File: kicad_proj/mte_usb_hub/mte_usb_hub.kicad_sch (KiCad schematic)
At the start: 3 parts

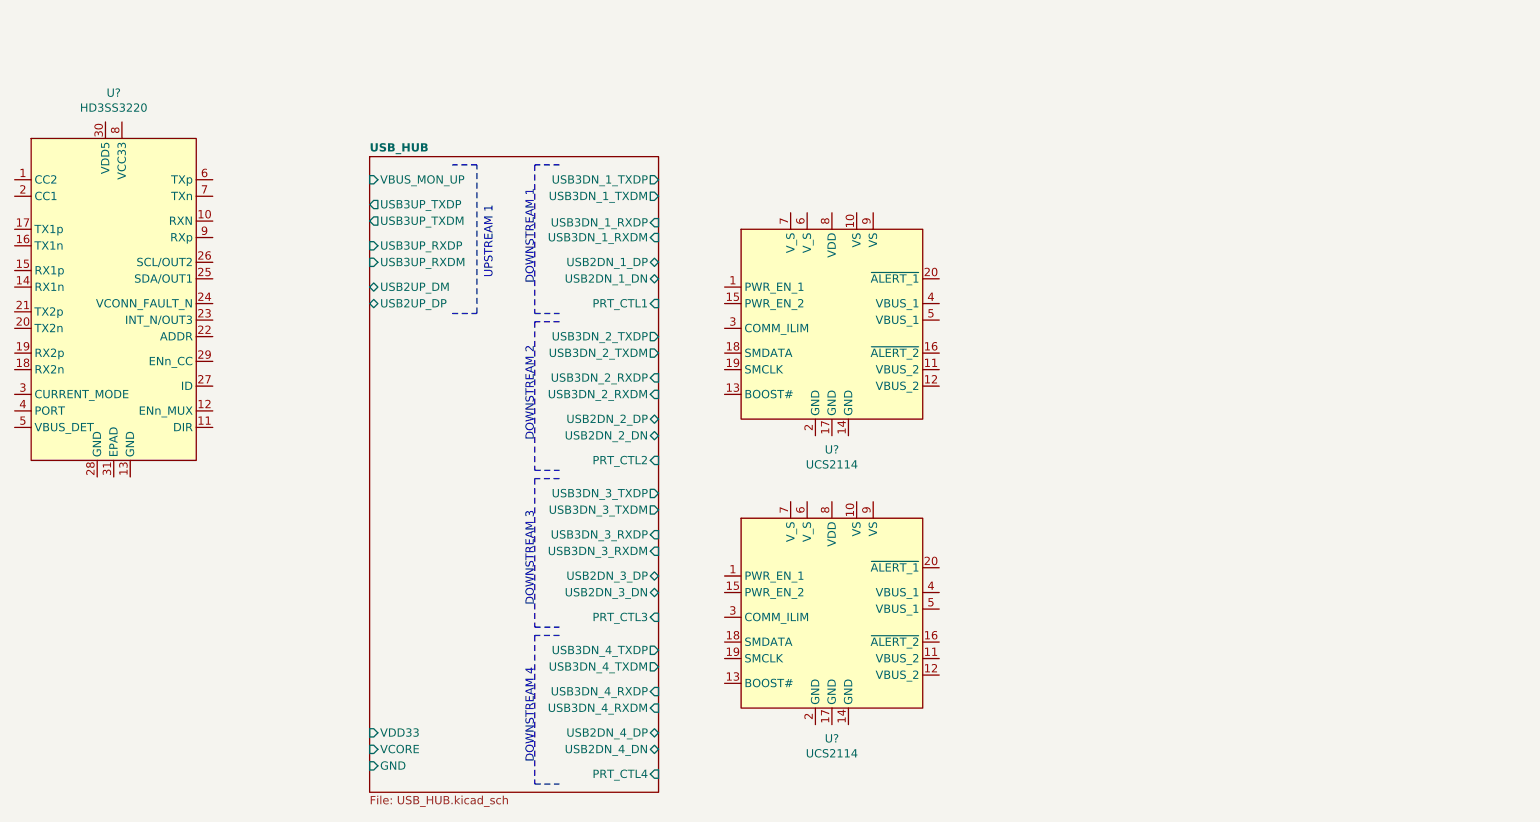
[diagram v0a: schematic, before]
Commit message: Finishes upstream USB setup
No power setup, no downstream ports setup
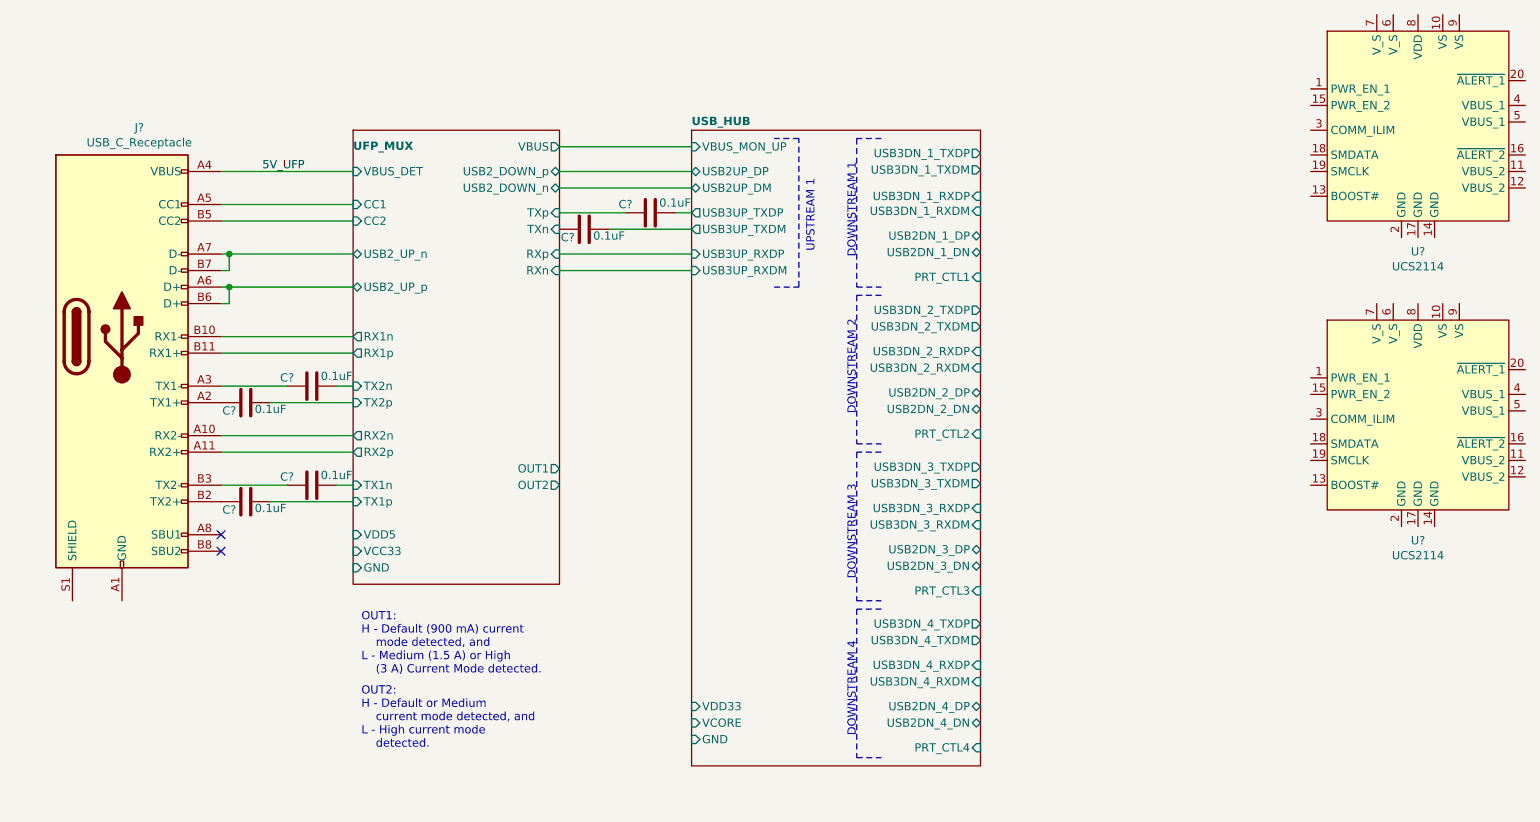
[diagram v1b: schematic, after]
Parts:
- removed U?: HD3SS3220, symbol mte_usb_hub:HD3SS3220
- added C? (x6): CC0402KRX5R7BB104, footprints:CAPACITOR_0402N, symbol mte_usb_hub:CC0402KRX5R7BB104
- added J?: USB_C_Receptacle, symbol Connector:USB_C_Receptacle
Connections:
- net USB_HUB/USB3UP_TXDM: now also C?.2
- net USB_HUB/USB3UP_TXDP: now also C?.2
- new net: C?.1, J?.B2 (TX2+)
- new net: C?.1, J?.A3 (TX1-)
- new net: J?.A1 (GND), J?.A12 (GND), J?.B1 (GND), J?.B12 (GND)
- new net: C?.1, J?.A2 (TX1+)
- new net: C?.1, J?.B3 (TX2-)
- new net 5V_UFP: J?.A4 (VBUS), J?.A9 (VBUS), J?.B4 (VBUS), J?.B9 (VBUS)
- new net UFP_MUX/CC1: J?.A5 (CC1)
- new net UFP_MUX/CC2: J?.B5 (CC2)
- new net UFP_MUX/RX1n: J?.B10 (RX1-)
- new net UFP_MUX/RX1p: J?.B11 (RX1+)
- new net UFP_MUX/RX2n: J?.A10 (RX2-)
- new net UFP_MUX/RX2p: J?.A11 (RX2+)
- new net UFP_MUX/TX1n: C?.2
- new net UFP_MUX/TX1p: C?.2
- new net UFP_MUX/TX2n: C?.2
- new net UFP_MUX/TX2p: C?.2
- new net UFP_MUX/TXn: C?.1
- new net UFP_MUX/TXp: C?.1
- new net UFP_MUX/USB2_UP_n: J?.A7 (D-), J?.B7 (D-)
- new net UFP_MUX/USB2_UP_p: J?.A6 (D+), J?.B6 (D+)
- no-connect marks 0 -> 2
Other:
- added sheet UFP_MUX (UFP_MUX.kicad_sch)
- note added: "OUT1: H - Default (900 mA) current mode detected, and L - Medium (1.5 A) or High (3 A) Current Mode detected."
- note added: "OUT2: H - Default or Medium current mode detected, and L - High current mode detected."
- moved on the sheet: U?

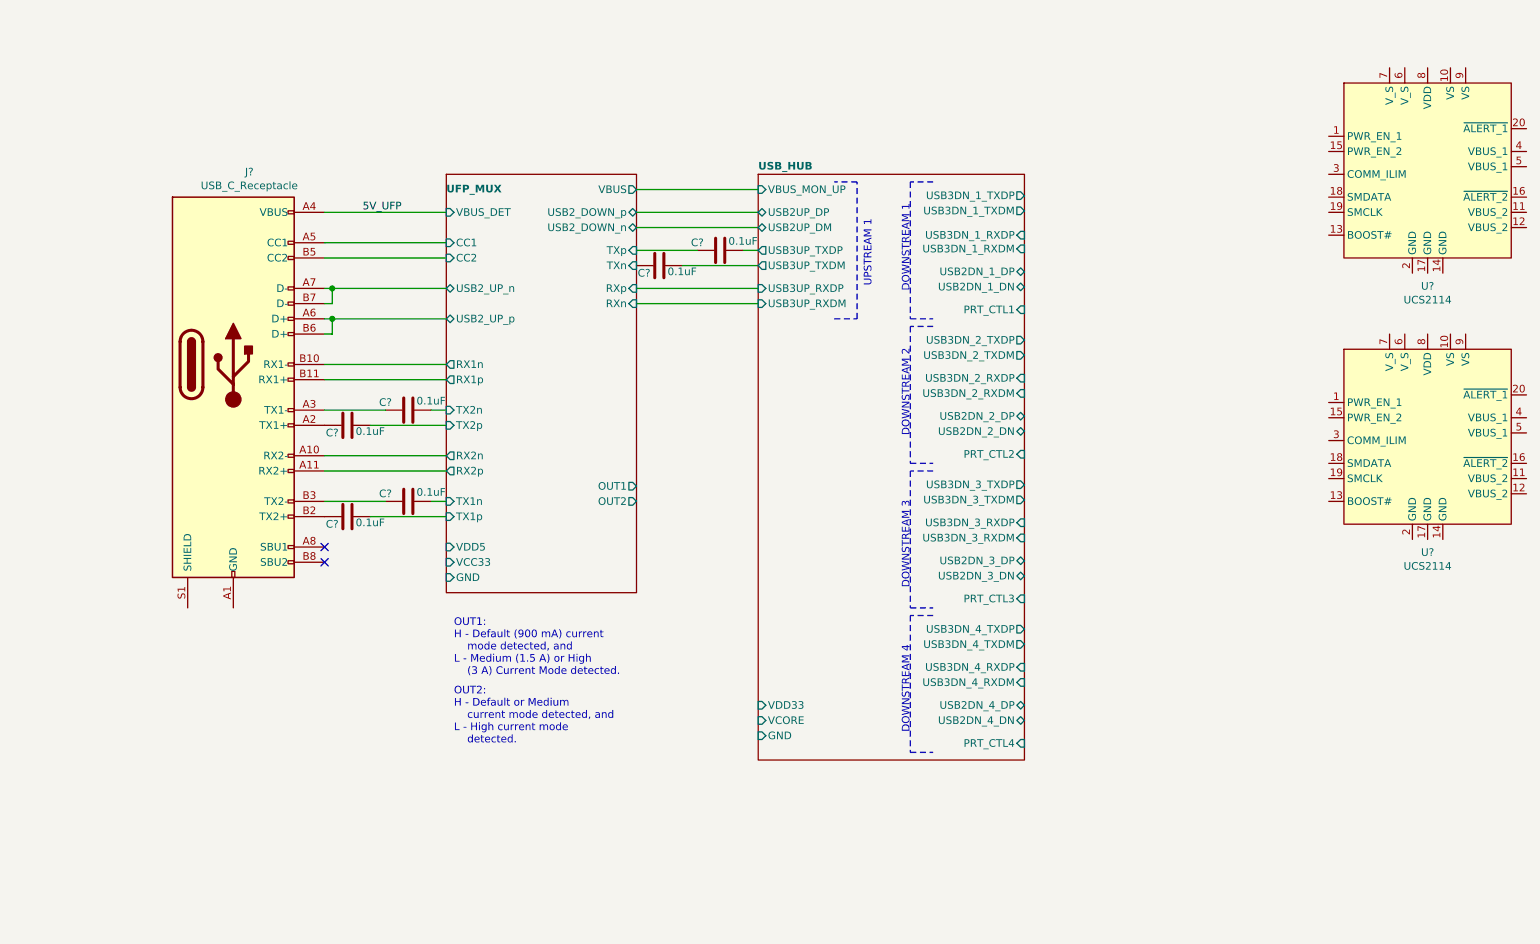
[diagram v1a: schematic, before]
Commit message: Starts downstream ports
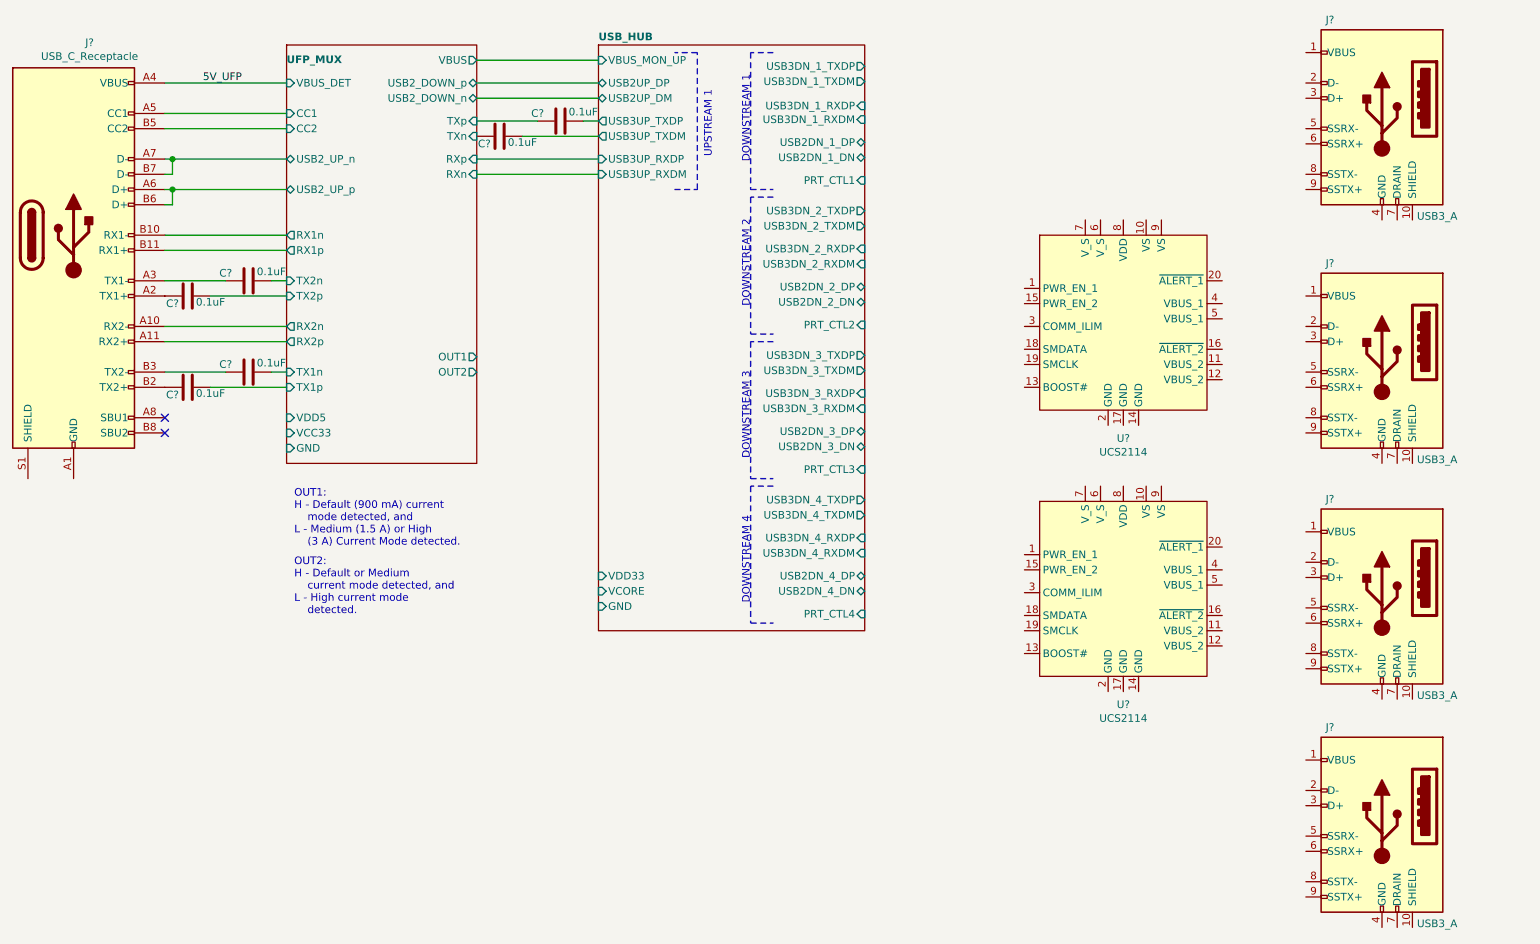
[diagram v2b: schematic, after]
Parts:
- added J? (x4): USB3_A, symbol Connector:USB3_A
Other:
- moved on the sheet: C?, J?, U?

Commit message: Final tweaks for the video
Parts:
- added C? (x8): CC0402KRX5R7BB104, footprints:CAPACITOR_0402N, symbol mte_usb_hub:CC0402KRX5R7BB104
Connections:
- net USB_HUB/USB3DN_1_TXDM: now also C?.1
- net USB_HUB/USB3DN_1_TXDP: now also C?.1
- net USB_HUB/USB3DN_2_TXDM: now also C?.1
- net USB_HUB/USB3DN_2_TXDP: now also C?.1
- net USB_HUB/USB3DN_3_TXDM: now also C?.1
- net USB_HUB/USB3DN_3_TXDP: now also C?.1
- net USB_HUB/USB3DN_4_TXDM: now also C?.1
- net USB_HUB/USB3DN_4_TXDP: now also C?.1
- net USB2DN_3_DN: now reaches J?.2 (D-)
- net USB2DN_3_DP: now reaches J?.3 (D+)
- net USB3DN_3_TXDN: now reaches J?.5 (SSRX-)
- net USB3DN_3_TXDN: now also C?.2
- net USB3DN_3_TXDP: now reaches J?.6 (SSRX+)
- net USB3DN_3_TXDP: now also C?.2
- net USB3DN_3_RXDN: now reaches J?.8 (SSTX-)
- net USB3DN_3_RXDP: now reaches J?.9 (SSTX+)
- net USB2DN_2_DN: now reaches J?.2 (D-)
- net USB2DN_2_DP: now reaches J?.3 (D+)
- net USB3DN_2_TXDN: now reaches J?.5 (SSRX-)
- net USB3DN_2_TXDN: now also C?.2
- net USB3DN_2_TXDP: now reaches J?.6 (SSRX+)
- net USB3DN_2_TXDP: now also C?.2
- net USB3DN_2_RXDN: now reaches J?.8 (SSTX-)
- net USB3DN_2_RXDP: now reaches J?.9 (SSTX+)
- net USB2DN_1_DN: now reaches J?.2 (D-)
- net USB2DN_1_DP: now reaches J?.3 (D+)
- net USB3DN_1_TXDN: now reaches J?.5 (SSRX-)
- net USB3DN_1_TXDN: now also C?.2
- net USB3DN_1_TXDP: now reaches J?.6 (SSRX+)
- net USB3DN_1_TXDP: now also C?.2
- net USB3DN_1_RXDN: now reaches J?.8 (SSTX-)
- net USB3DN_1_RXDP: now reaches J?.9 (SSTX+)
- net USB2DN_4_DN: now reaches J?.2 (D-)
- net USB2DN_4_DP: now reaches J?.3 (D+)
- net USB3DN_4_TXDN: now reaches J?.5 (SSRX-)
- net USB3DN_4_TXDN: now also C?.2
- net USB3DN_4_TXDP: now reaches J?.6 (SSRX+)
- net USB3DN_4_TXDP: now also C?.2
- net USB3DN_4_RXDN: now reaches J?.8 (SSTX-)
- net USB3DN_4_RXDP: now reaches J?.9 (SSTX+)
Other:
- moved on the sheet: C?, J?, U?

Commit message: Fixes Tx1/Tx2 being swapped from USB C UFP
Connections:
- net UFP_MUX/TX1n: now also C?.2; no longer C?.2
- net UFP_MUX/TX1p: now also C?.2; no longer C?.2
- net UFP_MUX/TX2n: now also C?.2; no longer C?.2
- net UFP_MUX/TX2p: now also C?.2; no longer C?.2
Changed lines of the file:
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@@
       (effects (font (size 1.27 1.27)) (justify left))
     )
-    (pin "TX1p" input (at 69.85 95.25 180)
+    (pin "TX1p" input (at 69.85 80.01 180)
       (effects (font (size 1.27 1.27)) (justify left))
     )
@@
       (effects (font (size 1.27 1.27)) (justify left))
     )
-    (pin "TX1n" input (at 69.85 92.71 180)
+    (pin "TX1n" input (at 69.85 77.47 180)
       (effects (font (size 1.27 1.27)) (justify left))
     )
-    (pin "TX2p" input (at 69.85 80.01 180)
+    (pin "TX2p" input (at 69.85 95.25 180)
       (effects (font (size 1.27 1.27)) (justify left))
     )
@@
       (effects (font (size 1.27 1.27)) (justify left))
     )
-    (pin "TX2n" input (at 69.85 77.47 180)
+    (pin "TX2n" input (at 69.85 92.71 180)
       (effects (font (size 1.27 1.27)) (justify left))
     )
